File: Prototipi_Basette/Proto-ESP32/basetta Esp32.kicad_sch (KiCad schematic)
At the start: 32 parts, among them J1 Conn_01x19, J2 Conn_01x19, J3 Conn_01x19, J4 Conn_01x19, J5 Screw_Terminal_01x02, J6 Conn_01x05, J7 Conn_01x02, Q1 BC547, Q2 BC547, Q3 IRF9540N, Q4 BC547, Q5 BC557, SW1 RESET, SW2 SET, U3 4013

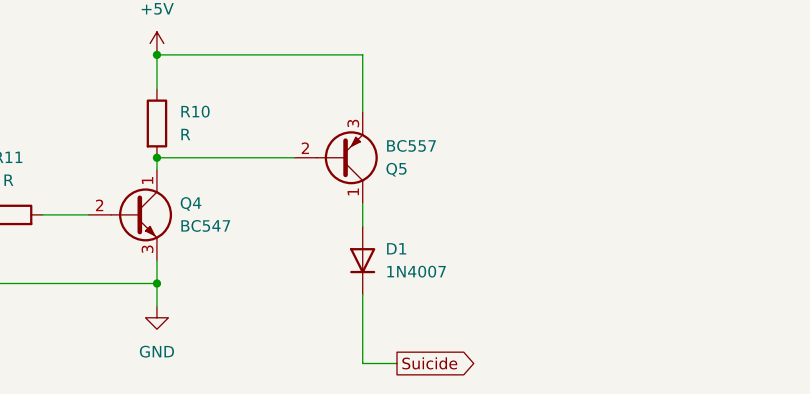
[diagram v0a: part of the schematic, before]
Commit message: Versione Stabile
Versione stabile con GND a piste, senza diodo nel suicide
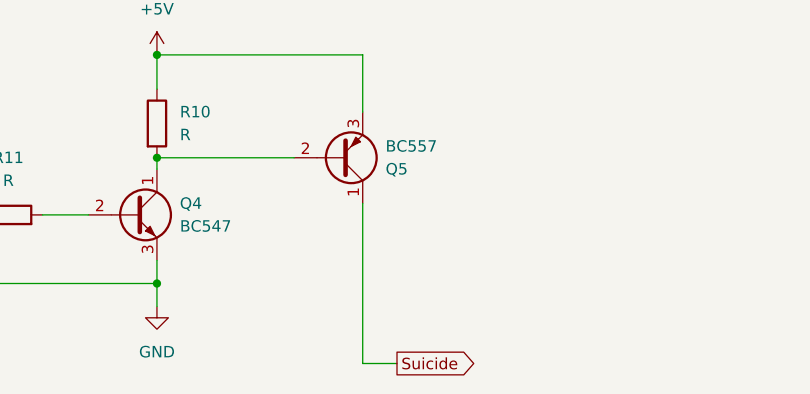
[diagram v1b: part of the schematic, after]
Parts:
- removed D1: 1N4007, Diode_THT:D_DO-41_SOD81_P7.62mm_Horizontal, symbol Diode:1N4007
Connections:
- net Suicide: now also Q5.1 (C)
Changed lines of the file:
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@@
 	(wire
 		(pts
-			(xy 182.88 142.24) (xy 182.88 144.78)
+			(xy 182.88 142.24) (xy 182.88 160.02)
 		)
 		(stroke
@@
 	(wire
 		(pts
-			(xy 182.88 160.02) (xy 182.88 152.4)
-		)
-		(stroke
-			(width 0)
-			(type default)
-		)
-	)
-	(wire
-		(pts
 			(xy 100.33 66.04) (xy 111.76 66.04)
 		)
@@
 					(unit 1)
 				)
-			)
-		)
-	)
-	(symbol
-		(lib_id "Diode:1N4007")
-		(at 182.88 148.59 90)
-		(unit 1)
-		(body_style 1)
-		(exclude_from_sim no)
-		(in_bom yes)
-		(on_board yes)
-		(in_pos_files yes)
-		(dnp no)
-		(fields_autoplaced yes)
-		(property "Reference" "D1"
-			(at 185.42 147.3199 90)
-			(show_name no)
-			(do_not_autoplace no)
-			(effects
-				(font
-					(size 1.27 1.27)
-				)
-				(justify right)
-			)
-		)
-		(property "Value" "1N4007"
-			(at 185.42 149.8599 90)
-			(show_name no)
-			(do_not_autoplace no)
-			(effects
-				(font
-					(size 1.27 1.27)
-				)
-				(justify right)
-			)
-		)
-		(property "Footprint" "Diode_THT:D_DO-41_SOD81_P7.62mm_Horizontal"
-			(at 187.325 148.59 0)
-			(hide yes)
-			(show_name no)
-			(do_not_autoplace no)
-			(effects
-				(font
-					(size 1.27 1.27)
-				)
-			)
-		)
-		(property "Datasheet" "http://www.vishay.com/docs/88503/1n4001.pdf"
-			(at 182.88 148.59 0)
-			(hide yes)
-			(show_name no)
-			(do_not_autoplace no)
-			(effects
-				(font
-					(size 1.27 1.27)
-				)
-			)
-		)
-		(property "Description" "1000V 1A General Purpose Rectifier Diode, DO-41"
-			(at 182.88 148.59 0)
-			(hide yes)
-			(show_name no)
-			(do_not_autoplace no)
-			(effects
-				(font
-					(size 1.27 1.27)
-				)
-			)
-		)
-		(property "Sim.Device" "D"
-			(at 182.88 148.59 0)
-			(hide yes)
-			(show_name no)
-			(do_not_autoplace no)
-			(effects
-				(font
-					(size 1.27 1.27)
-				)
-			)
-		)
-		(property "Sim.Pins" "1=K 2=A"
-			(at 182.88 148.59 0)
-			(hide yes)
-			(show_name no)
-			(do_not_autoplace no)
-			(effects
-				(font
-					(size 1.27 1.27)
-				)
-			)
-		)
-		(pin "2"
-		)
-		(pin "1"
-		)
-		(instances
-			(project "basetta Esp32"
-				(path "/7dff662c-5816-4f44-b24c-73522fc1f82f"
-					(reference "D1")
-					(unit 1)
-				)

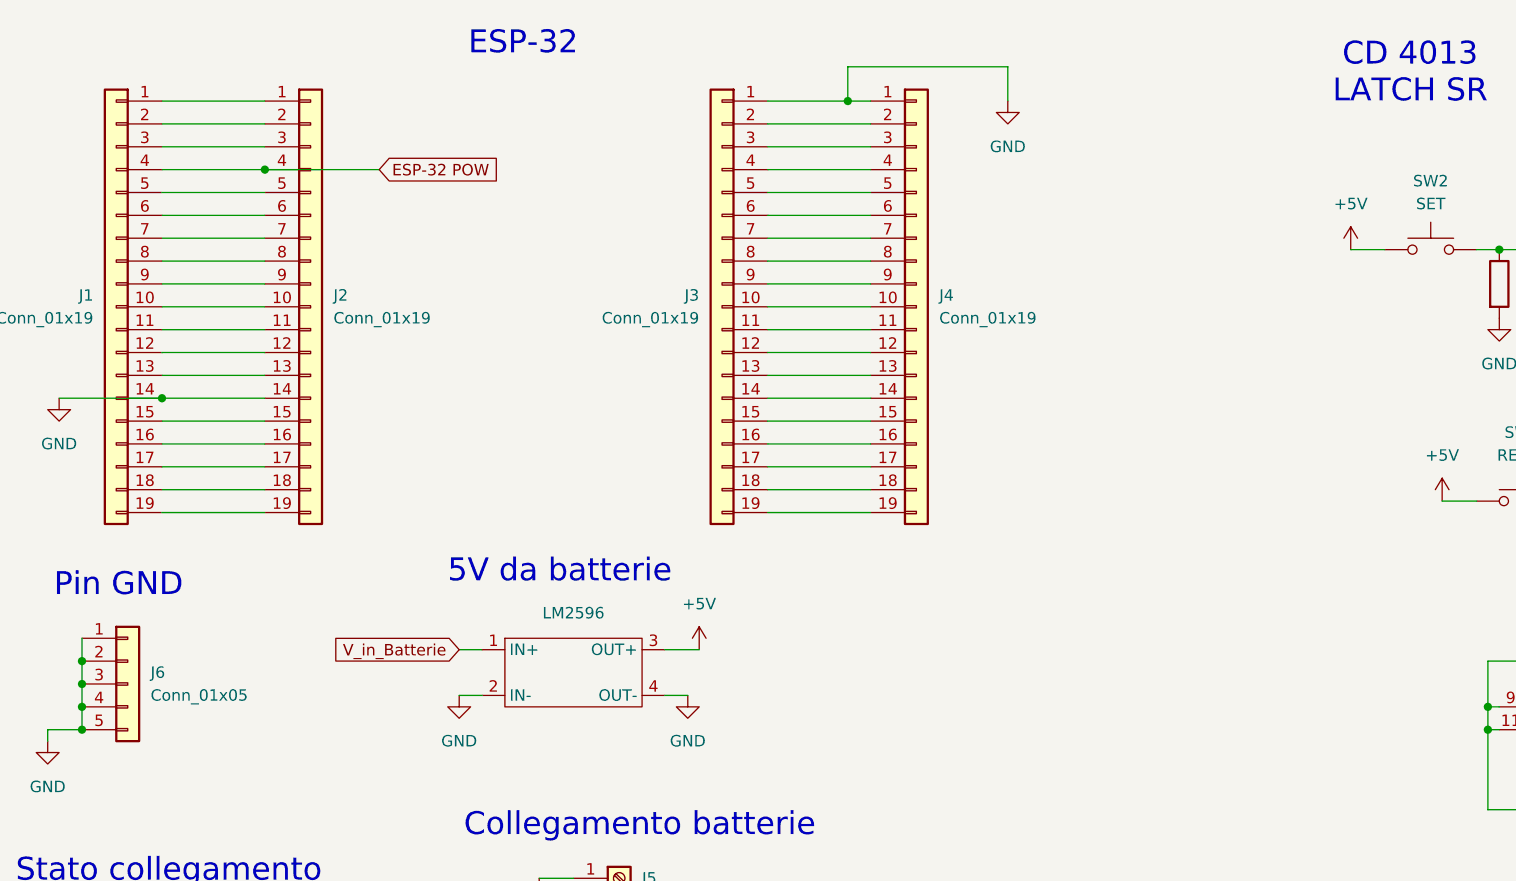
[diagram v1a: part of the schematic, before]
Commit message: Update KiCad PCB footprint positions and metadata
Adjust PCB layout: moved and rotated multiple footprints (resistors, DIP ICs, TO-92/TO-220 transistors, push button, switch, LM2596, etc.), corrected pad orientations (added/changed pad rotation angles), and realigned reference/value text positions on F.SilkS/F.Fab. Cleaned up silkscreen/fab geometry by reordering and fixing fp_line/fp_arc coordinates and updated many element UUIDs. Also fixed a net assignment (J1 Pin 1 -> +3V3). These changes align footprints and artwork for the revised board layout and ensure pads/text orientations match the new placement.
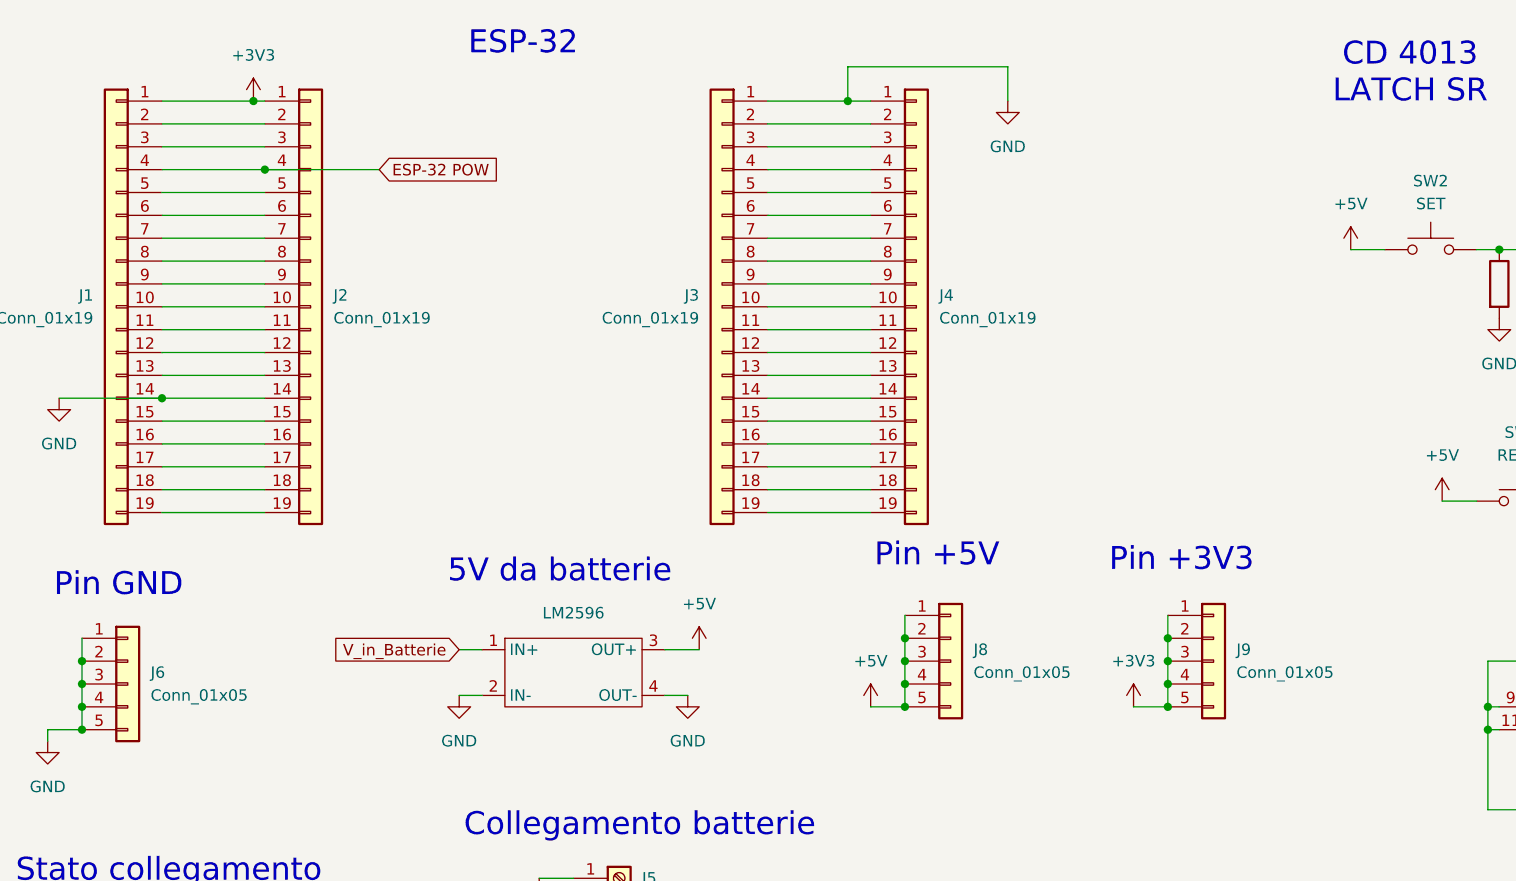
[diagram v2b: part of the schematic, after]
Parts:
- added J8, J9: Conn_01x05, Connector_PinSocket_2.54mm:PinSocket_1x05_P2.54mm_Vertical, symbol Connector_Generic:Conn_01x05
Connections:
- net +5V: now also J8.1 (Pin_1), J8.2 (Pin_2), J8.3 (Pin_3), J8.4 (Pin_4), J8.5 (Pin_5)
- net +3V3: now reaches J1.1 (Pin_1), J2.1 (Pin_1)
- net +3V3: now also J9.1 (Pin_1), J9.2 (Pin_2), J9.3 (Pin_3), J9.4 (Pin_4), J9.5 (Pin_5)
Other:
- note added: "Pin +3V3"
- note added: "Pin +5V"

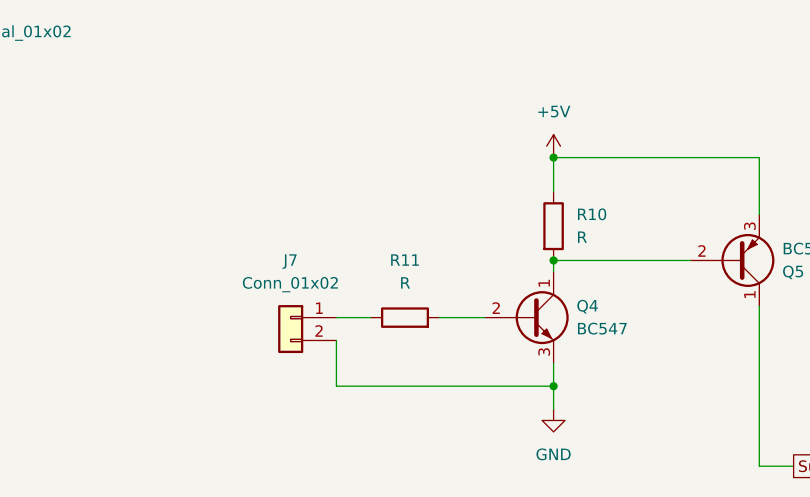
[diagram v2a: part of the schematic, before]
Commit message: Adjust PCB footprints, pads and routing
Move and reorient multiple footprints and update PCB geometry/metadata for the Proto-ESP32 layout. Changes include repositioning several resistors, TO-92 transistors, LEDs and a pin header; adding/adjusting pad rotation attributes (thru-hole pads set to 180 where needed); reordering and correcting silkscreen/fab lines and arcs; updating many footprint element UUIDs; and modifying F.Cu trace segments (notably for the +5V net) to match the new component placements. Also updated related project files and removed the KiCad .lck file.
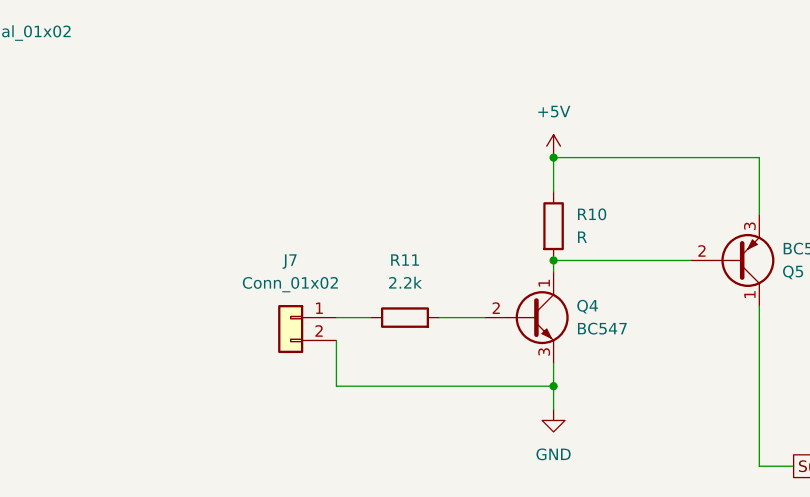
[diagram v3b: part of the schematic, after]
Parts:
- R11: value R -> 2.2k
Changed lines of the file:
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@@
 			)
 		)
-		(property "Value" "R"
+		(property "Value" "2.2k"
 			(at 143.51 139.7 90)
 			(show_name no)

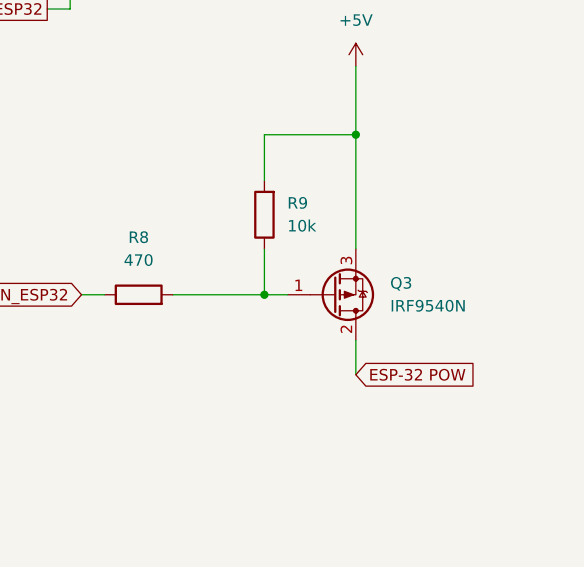
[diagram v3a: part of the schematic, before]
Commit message: Update MOSFET footprint, nets and refs
Modify PCB to replace a TO-92 footprint with a TO-220 horizontal power MOSFET (IRF9540N) and update related component properties, 3D model and datasheet. Fix pad nets (Q3-G -> Q6-G), adjust component placement (button Y pos), add units block to sheet instance, and update many footprint geometry, silk/fab/crtyd outlines and UUIDs. .kicad_pcb (and associated project files) updated to reflect new pad sizes, drills, pad ordering and property metadata for Q4/Q5/Q6 and related footprints.
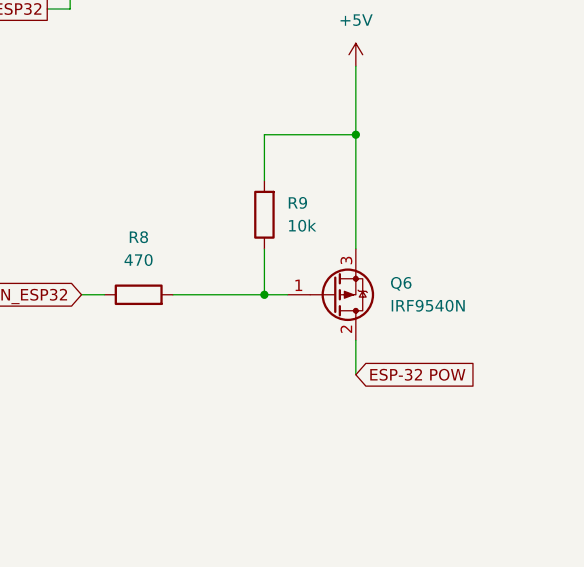
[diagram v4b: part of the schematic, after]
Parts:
- removed Q3: IRF9540N, Package_TO_SOT_THT:TO-220-3_Vertical, symbol Transistor_FET:IRF9540N
- added Q6: IRF9540N, Package_TO_SOT_THT:TO-220-3_Horizontal_TabDown, symbol Transistor_FET:IRF9540N
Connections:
- net +5V: now also Q6.3 (S)
- net ESP-32 POW: now also Q6.2 (D)
- net at R8.2, R9.1: now also Q6.1 (G)
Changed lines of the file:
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@@
 	)
 	(junction
-		(at 144.78 90.17)
+		(at 250.19 111.76)
 		(diameter 0)
 		(color 0 0 0 0)
 	)
 	(junction
-		(at 181.61 39.37)
+		(at 144.78 90.17)
 		(diameter 0)
 		(color 0 0 0 0)
 	)
 	(junction
-		(at 260.35 93.98)
+		(at 181.61 39.37)
 		(diameter 0)
 		(color 0 0 0 0)
@@
 	)
 	(junction
-		(at 250.19 111.76)
+		(at 115.57 82.55)
 		(diameter 0)
 		(color 0 0 0 0)
 	)
 	(junction
-		(at 115.57 82.55)
+		(at 260.35 93.98)
 		(diameter 0)
 		(color 0 0 0 0)
@@
 	)
 	(symbol
+		(lib_id "Transistor_FET:IRF9540N")
+		(at 257.81 111.76 0)
+		(mirror x)
+		(unit 1)
+		(body_style 1)
+		(exclude_from_sim no)
+		(in_bom yes)
+		(on_board yes)
+		(in_pos_files yes)
+		(dnp no)
+		(fields_autoplaced yes)
+		(property "Reference" "Q6"
+			(at 264.16 110.4899 0)
+			(show_name no)
+			(do_not_autoplace no)
+			(effects
+				(font
+					(size 1.27 1.27)
+				)
+				(justify left)
+			)
+		)
+		(property "Value" "IRF9540N"
+			(at 264.16 113.0299 0)
+			(show_name no)
+			(do_not_autoplace no)
+			(effects
+				(font
+					(size 1.27 1.27)
+				)
+				(justify left)
+			)
+		)
+		(property "Footprint" "Package_TO_SOT_THT:TO-220-3_Horizontal_TabDown"
+			(at 262.89 109.855 0)
+			(hide yes)
+			(show_name no)
+			(do_not_autoplace no)
+			(effects
+				(font
+					(size 1.27 1.27)
+					(italic yes)
+				)
+				(justify left)
+			)
+		)
+		(property "Datasheet" "http://www.irf.com/product-info/datasheets/data/irf9540n.pdf"
+			(at 262.89 107.95 0)
+			(hide yes)
+			(show_name no)
+			(do_not_autoplace no)
+			(effects
+				(font
+					(size 1.27 1.27)
+				)
+				(justify left)
+			)
+		)
+		(property "Description" "-23A Id, -100V Vds, 117mOhm Rds, P-Channel HEXFET Power MOSFET, TO-220"
+			(at 257.81 111.76 0)
+			(hide yes)
+			(show_name no)
+			(do_not_autoplace no)
+			(effects
+				(font
+					(size 1.27 1.27)
+				)
+			)
+		)
+		(pin "2"
+		)
+		(pin "3"
+		)
+		(pin "1"
+		)
+		(instances
+			(project "basetta Esp32"
+				(path "/7dff662c-5816-4f44-b24c-73522fc1f82f"
+					(reference "Q6")
+					(unit 1)
+				)
+			)
+		)
+	)
+	(symbol
 		(lib_id "power:+5V")
 		(at 92.71 83.82 0)
@@
 					(unit 1)
 				)
-			)
-		)
-	)
-	(symbol
-		(lib_id "Transistor_FET:IRF9540N")
-		(at 257.81 111.76 0)
-		(mirror x)
-		(unit 1)
-		(body_style 1)
-		(exclude_from_sim no)
-		(in_bom yes)
-		(on_board yes)
-		(in_pos_files yes)
-		(dnp no)
-		(fields_autoplaced yes)
-		(property "Reference" "Q3"
-			(at 264.16 110.4899 0)
-			(show_name no)
-			(do_not_autoplace no)
-			(effects
-				(font
-					(size 1.27 1.27)
-				)
-				(justify left)
-			)
-		)
-		(property "Value" "IRF9540N"
-			(at 264.16 113.0299 0)
-			(show_name no)
-			(do_not_autoplace no)
-			(effects
-				(font
-					(size 1.27 1.27)
-				)
-				(justify left)
-			)
-		)
-		(property "Footprint" "Package_TO_SOT_THT:TO-220-3_Vertical"
-			(at 262.89 109.855 0)
-			(hide yes)
-			(show_name no)
-			(do_not_autoplace no)
-			(effects
-				(font
-					(size 1.27 1.27)
-					(italic yes)
-				)
-				(justify left)
-			)
-		)
-		(property "Datasheet" "http://www.irf.com/product-info/datasheets/data/irf9540n.pdf"
-			(at 262.89 107.95 0)
-			(hide yes)
-			(show_name no)
-			(do_not_autoplace no)
-			(effects
-				(font
-					(size 1.27 1.27)
-				)
-				(justify left)
-			)
-		)
-		(property "Description" "-23A Id, -100V Vds, 117mOhm Rds, P-Channel HEXFET Power MOSFET, TO-220"
-			(at 257.81 111.76 0)
-			(hide yes)
-			(show_name no)
-			(do_not_autoplace no)
-			(effects
-				(font
-					(size 1.27 1.27)
-				)
-			)
-		)
-		(pin "2"
-		)
-		(pin "1"
-		)
-		(pin "3"
-		)
-		(instances
-			(project "basetta Esp32"
-				(path "/7dff662c-5816-4f44-b24c-73522fc1f82f"
-					(reference "Q3")
-					(unit 1)
-				)
